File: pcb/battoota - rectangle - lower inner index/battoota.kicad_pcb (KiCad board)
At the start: 2 copper layers, 123.9 x 90 mm, 38 parts

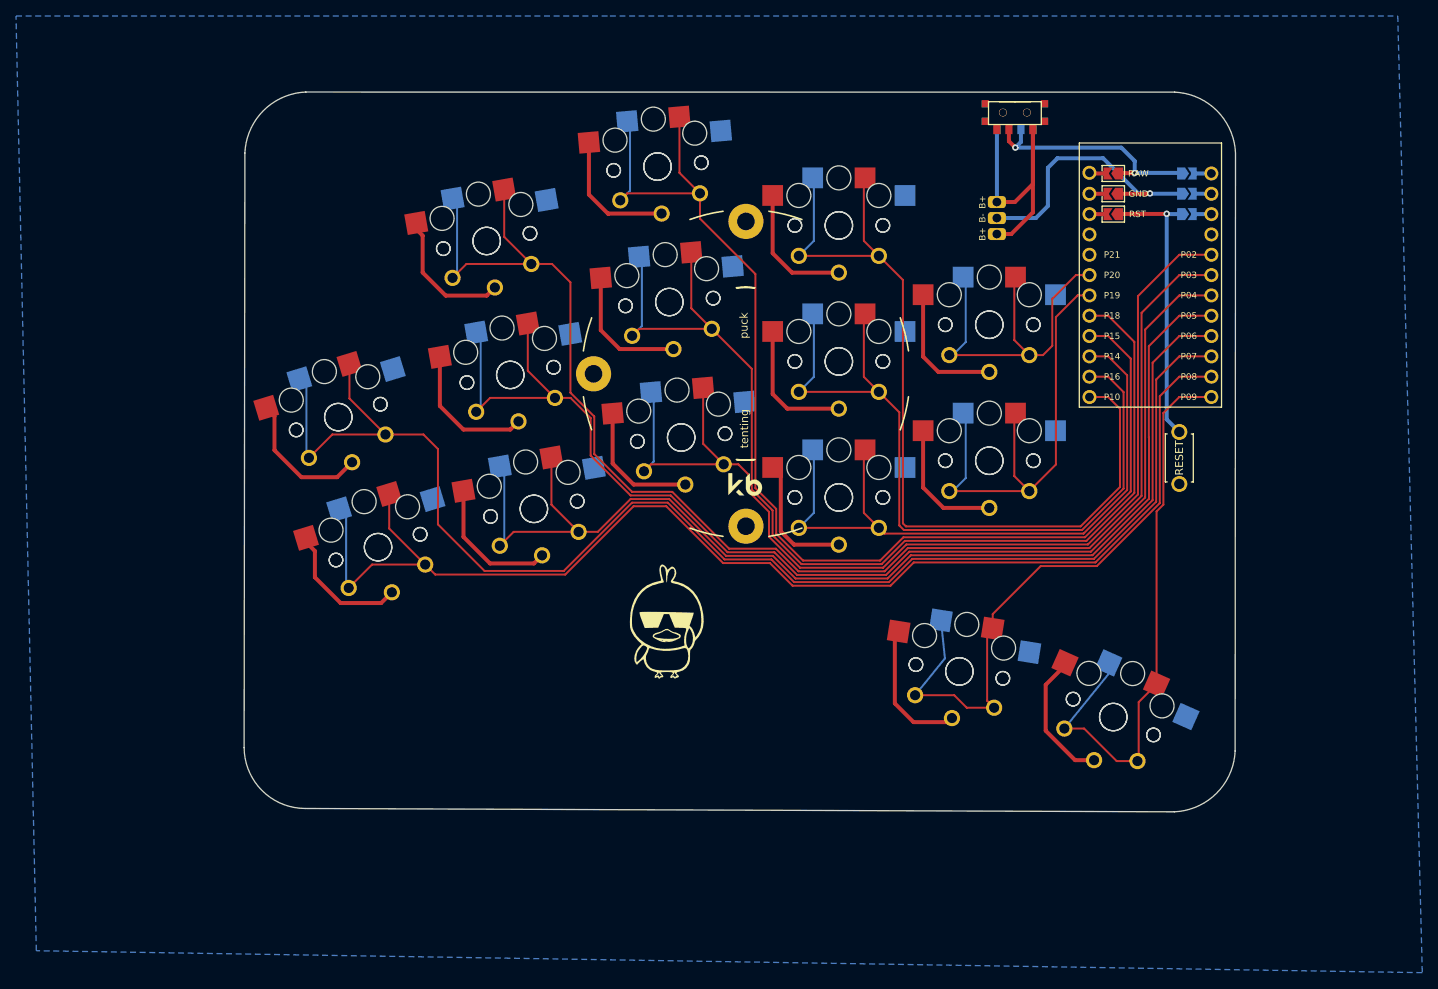
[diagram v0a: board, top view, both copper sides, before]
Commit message: more uniform rectangle for battoota
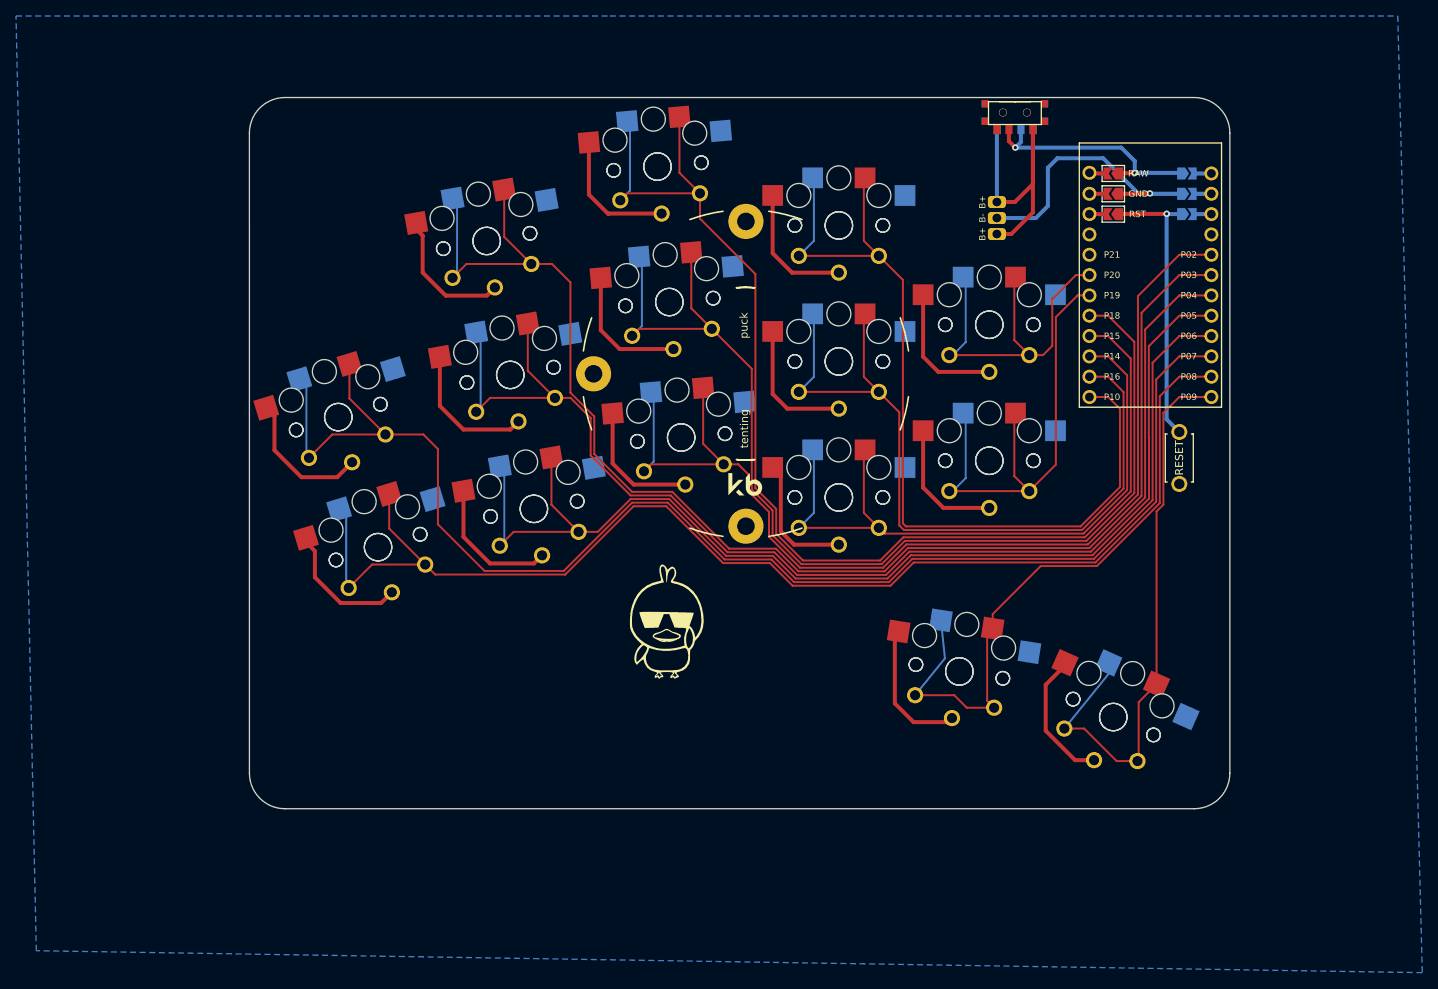
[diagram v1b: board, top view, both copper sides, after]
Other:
- board size 123.9 x 90 mm -> 122.6 x 88.9 mm
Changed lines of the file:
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@@
       ) (layer "B.SilkS") (width 0) (fill solid))
   )
-  (gr_line (start 157.373271 -123.349983) (end 48.779334 -123.36481) (layer "Edge.Cuts") (width 0.15))
-  (gr_arc (start 164.948263 -41.009332) (mid 162.628869 -35.71328) (end 157.334791 -33.389332) (layer "Edge.Cuts") (width 0.15))
-  (gr_line (start 41.165862 -115.74481) (end 41.071041 -41.428254) (layer "Edge.Cuts") (width 0.15))
-  (gr_arc (start 48.691041 -33.808254) (mid 43.311577 -36.04879) (end 41.071041 -41.428254) (layer "Edge.Cuts") (width 0.15))
-  (gr_line (start 164.948263 -41.009332) (end 164.993271 -115.736511) (layer "Edge.Cuts") (width 0.15))
-  (gr_line (start 157.334791 -33.389332) (end 48.691041 -33.808254) (layer "Edge.Cuts") (width 0.15))
-  (gr_arc (start 157.373271 -123.349983) (mid 162.669331 -121.030581) (end 164.993271 -115.736511) (layer "Edge.Cuts") (width 0.15))
-  (gr_arc (start 41.165862 -115.74481) (mid 43.485264 -121.04087) (end 48.779334 -123.36481) (layer "Edge.Cuts") (width 0.15))
+  (gr_arc (start 41.729239 -118.234208) (mid 43.031149 -121.377298) (end 46.174239 -122.679208) (layer "Edge.Cuts") (width 0.05))
+  (gr_arc (start 46.177881 -33.776344) (mid 43.034791 -35.078254) (end 41.732881 -38.221344) (layer "Edge.Cuts") (width 0.05))
+  (gr_arc (start 164.284275 -38.222993) (mid 162.982364 -35.079906) (end 159.839275 -33.777993) (layer "Edge.Cuts") (width 0.05))
+  (gr_line (start 164.284275 -38.222993) (end 164.287881 -118.231344) (layer "Edge.Cuts") (width 0.05))
+  (gr_line (start 41.729239 -118.234208) (end 41.732881 -38.221344) (layer "Edge.Cuts") (width 0.05))
+  (gr_line (start 159.842881 -122.676344) (end 46.174239 -122.679208) (layer "Edge.Cuts") (width 0.05))
+  (gr_arc (start 159.842881 -122.676344) (mid 162.985974 -121.374437) (end 164.287881 -118.231344) (layer "Edge.Cuts") (width 0.05))
+  (gr_line (start 46.177881 -33.776344) (end 159.839275 -33.777993) (layer "Edge.Cuts") (width 0.05))
   (segment (start 147.293059 -65.010791) (end 124.592825 -65.010791) (width 0.25) (layer "F.Cu") (net 1))
   (segment (start 124.592825 -65.010791) (end 121.686138 -62.104105) (width 0.25) (layer "F.Cu") (net 1))

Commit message: move jst location on lower index
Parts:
- moved PAD1 3.09 mm to (135.1, -110.7)
- moved T1 0.09 mm to (137.4, -120.7)
- moved T2 0.09 mm to (137.4, -120.7)
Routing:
- net Braw: track 37.5 -> 28.9 mm
- net GND: track 289.9 -> 285.8 mm
